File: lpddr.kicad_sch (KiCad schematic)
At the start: 37 parts, among them U1 MPFS250T-FCVG484, U12 MT53D512M32D2_WFBGA

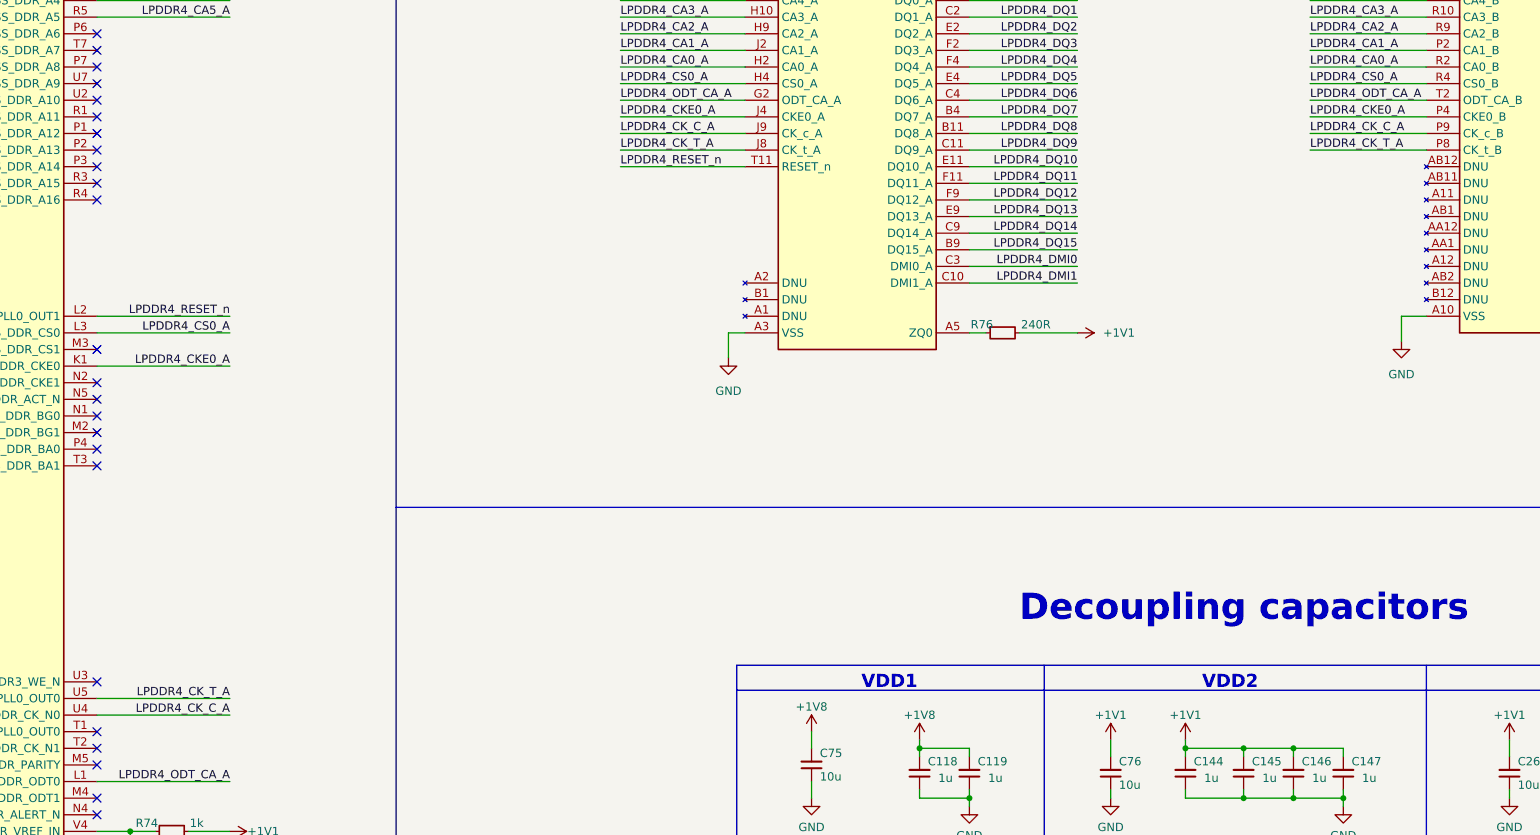
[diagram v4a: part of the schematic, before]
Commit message: [#56715] LPDDR4 match LS signals
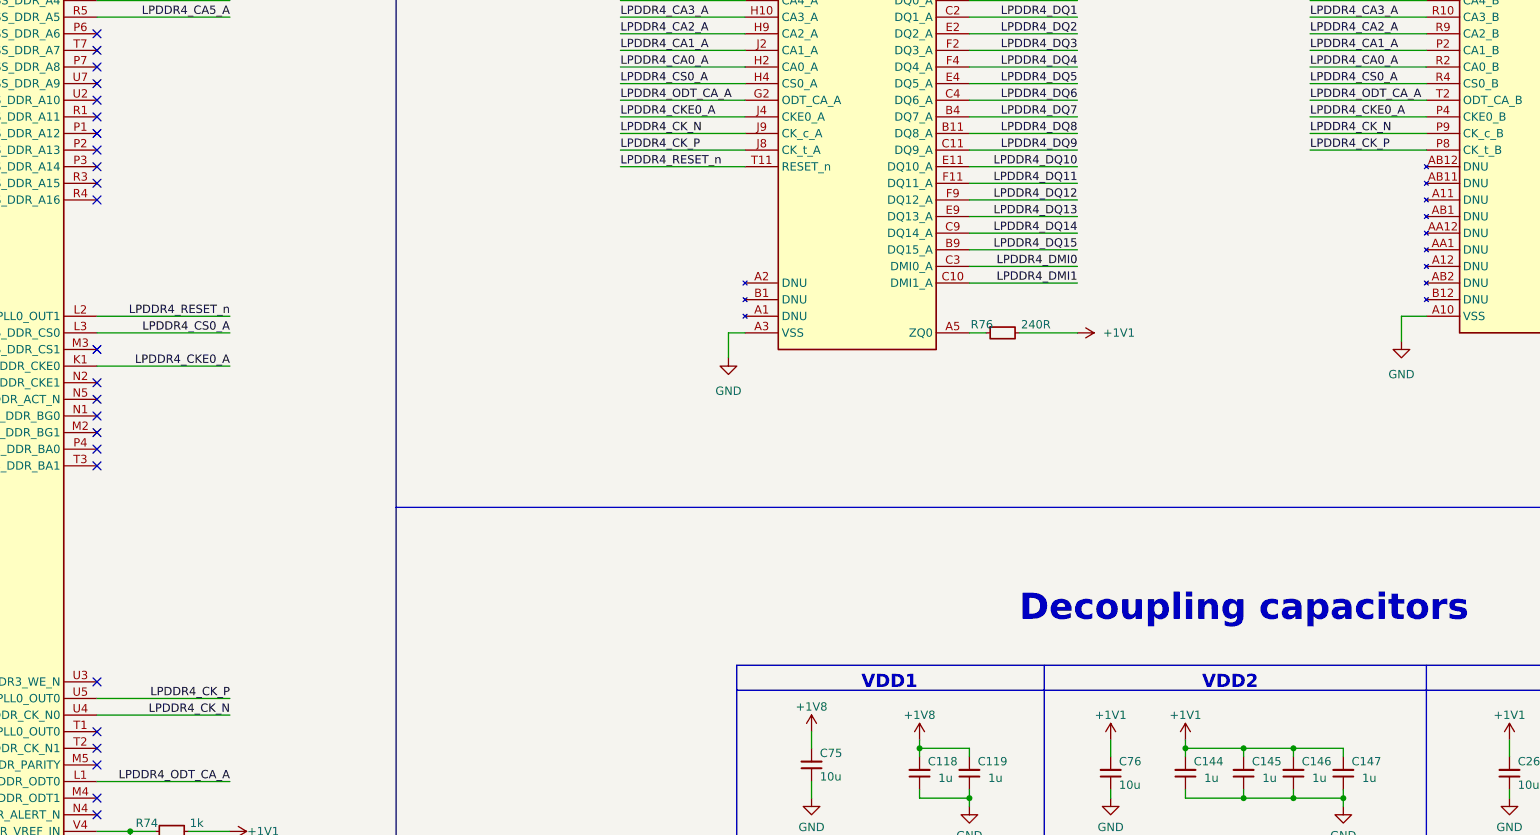
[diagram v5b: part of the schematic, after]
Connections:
- net LPDDR4_CK_C_A renamed LPDDR4_CK_N
- net LPDDR4_CK_T_A renamed LPDDR4_CK_P
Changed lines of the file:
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@@
-    (effects (font (size 1.27 1.27)) (justify left bottom))
-  )
-  (label "LPDDR4_CK_C_A" (at 312.42 96.52 0) (fields_autoplaced)
     (effects (font (size 1.27 1.27)) (justify left bottom))
   )
@@
     (effects (font (size 1.27 1.27)) (justify left bottom))
   )
+  (label "LPDDR4_CK_N" (at 207.01 96.52 0) (fields_autoplaced)
+    (effects (font (size 1.27 1.27)) (justify left bottom))
+  )
   (label "LPDDR4_DQ21" (at 45.72 139.7 0) (fields_autoplaced)
     (effects (font (size 1.27 1.27)) (justify left bottom))
@@
     (effects (font (size 1.27 1.27)) (justify left bottom))
   )
-  (label "LPDDR4_CK_C_A" (at 207.01 96.52 0) (fields_autoplaced)
-    (effects (font (size 1.27 1.27)) (justify left bottom))
-  )
-  (label "LPDDR4_CK_T_A" (at 312.42 99.06 0) (fields_autoplaced)
-    (effects (font (size 1.27 1.27)) (justify left bottom))
-  )
   (label "LPDDR4_DQS0_P" (at 276.86 68.58 180) (fields_autoplaced)
     (effects (font (size 1.27 1.27)) (justify right bottom))
@@
     (effects (font (size 1.27 1.27)) (justify right bottom))
   )
+  (label "LPDDR4_CK_N" (at 312.42 96.52 0) (fields_autoplaced)
+    (effects (font (size 1.27 1.27)) (justify left bottom))
+  )
   (label "LPDDR4_RESET_n" (at 207.01 101.6 0) (fields_autoplaced)
     (effects (font (size 1.27 1.27)) (justify left bottom))
@@
     (effects (font (size 1.27 1.27)) (justify left bottom))
   )
+  (label "LPDDR4_CK_P" (at 312.42 99.06 0) (fields_autoplaced)
+    (effects (font (size 1.27 1.27)) (justify left bottom))
+  )
   (label "LPDDR4_DQ12" (at 45.72 106.68 0) (fields_autoplaced)
     (effects (font (size 1.27 1.27)) (justify left bottom))
@@
     (effects (font (size 1.27 1.27)) (justify right bottom))
   )
+  (label "LPDDR4_CK_P" (at 207.01 99.06 0) (fields_autoplaced)
+    (effects (font (size 1.27 1.27)) (justify left bottom))
+  )
   (label "LPDDR4_DQ23" (at 381 93.98 180) (fields_autoplaced)
     (effects (font (size 1.27 1.27)) (justify right bottom))
@@
     (effects (font (size 1.27 1.27)) (justify left bottom))
   )
-  (label "LPDDR4_CK_T_A" (at 207.01 99.06 0) (fields_autoplaced)
-    (effects (font (size 1.27 1.27)) (justify left bottom))
-  )
   (label "LPDDR4_DQ25" (at 45.72 160.02 0) (fields_autoplaced)
     (effects (font (size 1.27 1.27)) (justify left bottom))
@@
     (effects (font (size 1.27 1.27)) (justify left bottom))
   )
-  (label "LPDDR4_CK_C_A" (at 147.32 185.42 180) (fields_autoplaced)
+  (label "LPDDR4_CK_N" (at 147.32 185.42 180) (fields_autoplaced)
     (effects (font (size 1.27 1.27)) (justify right bottom))
   )
@@
     (effects (font (size 1.27 1.27)) (justify right bottom))
   )
-  (label "LPDDR4_CK_T_A" (at 147.32 182.88 180) (fields_autoplaced)
-    (effects (font (size 1.27 1.27)) (justify right bottom))
-  )
+  (label "LPDDR4_CK_P" (at 147.32 182.88 180) (fields_autoplaced)
+    (effects (font (size 1.27 1.27)) (justify right bottom))
+  )

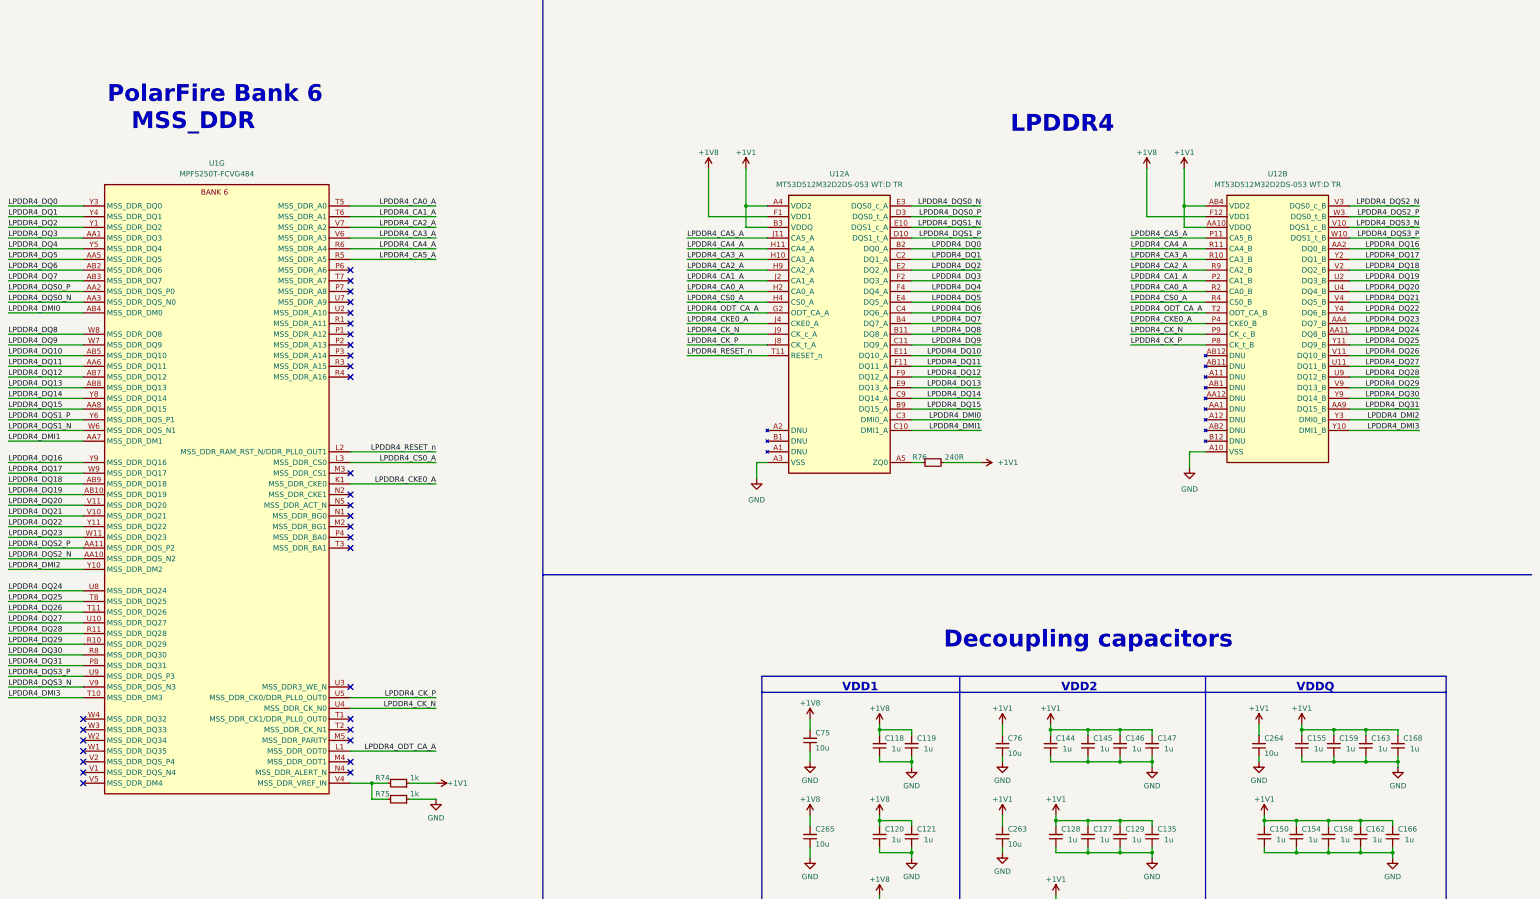
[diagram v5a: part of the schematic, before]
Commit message: [#57505] Start reworking schematic to hierarchical structure
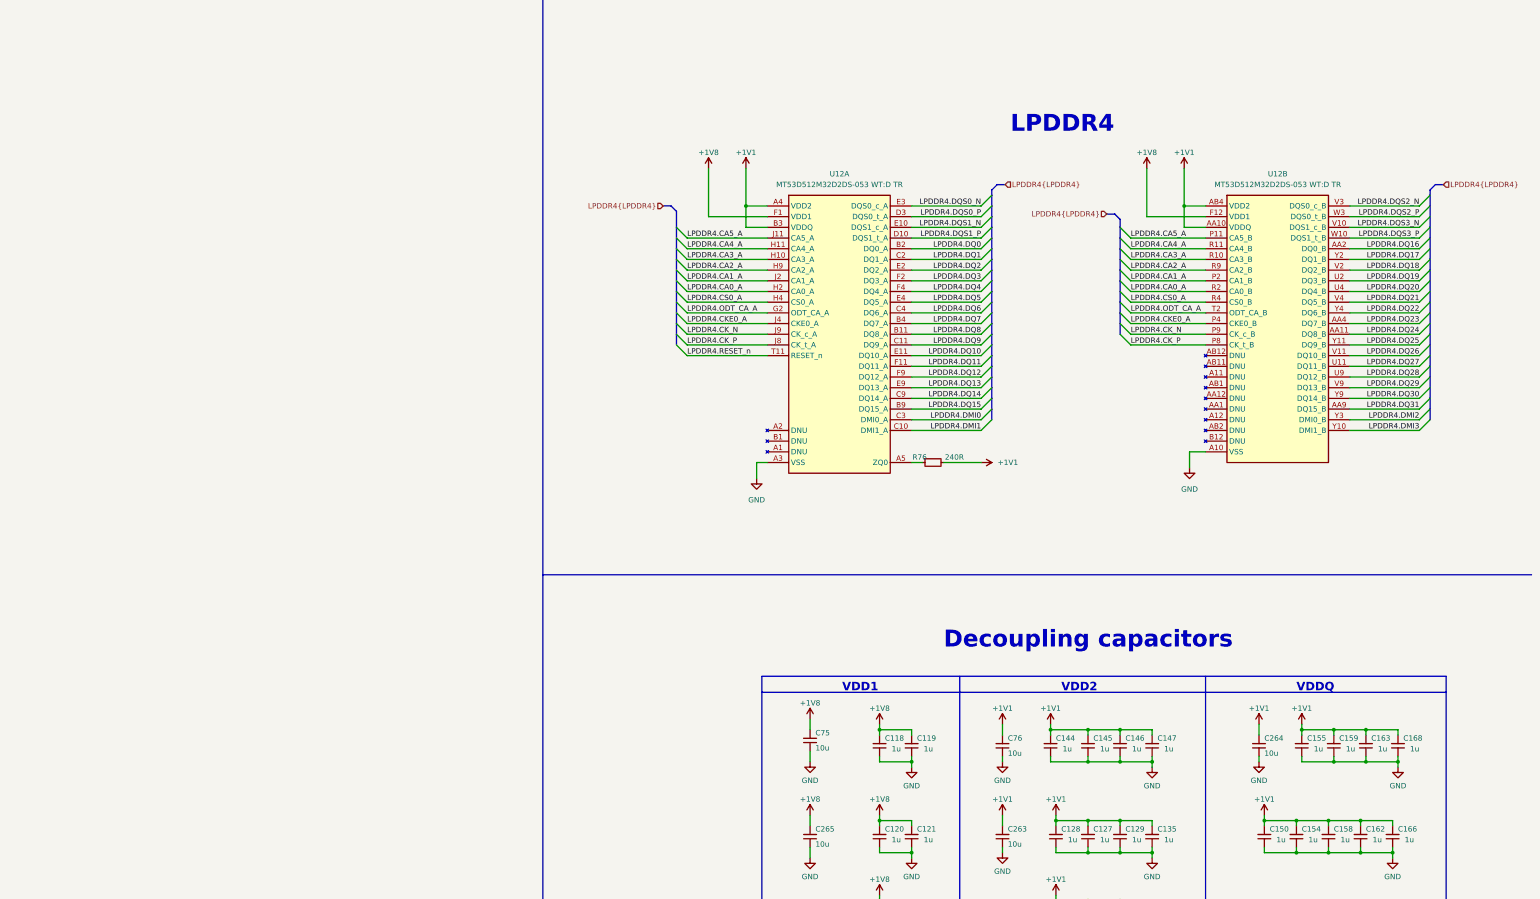
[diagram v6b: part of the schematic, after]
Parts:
- removed R74, R75: R_1k_0402, antmicro-footprints:R_0402_1005Metric, symbol antmicroResistors0402:R_1k_0402
- removed U1: MPFS250T-FCVG484, antmicro-footprints:BGA-484_19x19mm_Layout22x22_P0.8mm-microchip-technology-mpfs250t-fcvg484, symbol antmicroFPGAChips:MPFS250T-FCVG484
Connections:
- net LPDDR4_CA0_A renamed LPDDR4.CA0_A
- net LPDDR4_CA1_A renamed LPDDR4.CA1_A
- net LPDDR4_CA2_A renamed LPDDR4.CA2_A
- net LPDDR4_CA3_A renamed LPDDR4.CA3_A
- net LPDDR4_CA4_A renamed LPDDR4.CA4_A
- net LPDDR4_CA5_A renamed LPDDR4.CA5_A
- net LPDDR4_CKE0_A renamed LPDDR4.CKE0_A
- net LPDDR4_CK_N renamed LPDDR4.CK_N
- net LPDDR4_CK_P renamed LPDDR4.CK_P
- net LPDDR4_CS0_A renamed LPDDR4.CS0_A
- net LPDDR4_DMI0 renamed LPDDR4.DMI0
- net LPDDR4_DMI1 renamed LPDDR4.DMI1
- net LPDDR4_DMI2 renamed LPDDR4.DMI2
- net LPDDR4_DMI3 renamed LPDDR4.DMI3
- net LPDDR4_DQ0 renamed LPDDR4.DQ0
- net LPDDR4_DQ1 renamed LPDDR4.DQ1
- net LPDDR4_DQ10 renamed LPDDR4.DQ10
- net LPDDR4_DQ11 renamed LPDDR4.DQ11
- net LPDDR4_DQ12 renamed LPDDR4.DQ12
- net LPDDR4_DQ13 renamed LPDDR4.DQ13
- net LPDDR4_DQ14 renamed LPDDR4.DQ14
- net LPDDR4_DQ15 renamed LPDDR4.DQ15
- net LPDDR4_DQ16 renamed LPDDR4.DQ16
- net LPDDR4_DQ17 renamed LPDDR4.DQ17
- net LPDDR4_DQ18 renamed LPDDR4.DQ18
- net LPDDR4_DQ19 renamed LPDDR4.DQ19
- net LPDDR4_DQ2 renamed LPDDR4.DQ2
- net LPDDR4_DQ20 renamed LPDDR4.DQ20
- net LPDDR4_DQ21 renamed LPDDR4.DQ21
- net LPDDR4_DQ22 renamed LPDDR4.DQ22
- net LPDDR4_DQ23 renamed LPDDR4.DQ23
- net LPDDR4_DQ24 renamed LPDDR4.DQ24
- net LPDDR4_DQ25 renamed LPDDR4.DQ25
- net LPDDR4_DQ26 renamed LPDDR4.DQ26
- net LPDDR4_DQ27 renamed LPDDR4.DQ27
- net LPDDR4_DQ28 renamed LPDDR4.DQ28
- net LPDDR4_DQ29 renamed LPDDR4.DQ29
- net LPDDR4_DQ3 renamed LPDDR4.DQ3
- net LPDDR4_DQ30 renamed LPDDR4.DQ30
- net LPDDR4_DQ31 renamed LPDDR4.DQ31
- net LPDDR4_DQ4 renamed LPDDR4.DQ4
- net LPDDR4_DQ5 renamed LPDDR4.DQ5
- net LPDDR4_DQ6 renamed LPDDR4.DQ6
- net LPDDR4_DQ7 renamed LPDDR4.DQ7
- net LPDDR4_DQ8 renamed LPDDR4.DQ8
- net LPDDR4_DQ9 renamed LPDDR4.DQ9
- net LPDDR4_DQS0_N renamed LPDDR4.DQS0_N
- net LPDDR4_DQS0_P renamed LPDDR4.DQS0_P
- net LPDDR4_DQS1_N renamed LPDDR4.DQS1_N
- net LPDDR4_DQS1_P renamed LPDDR4.DQS1_P
- net LPDDR4_DQS2_N renamed LPDDR4.DQS2_N
- net LPDDR4_DQS2_P renamed LPDDR4.DQS2_P
- net LPDDR4_DQS3_N renamed LPDDR4.DQS3_N
- net LPDDR4_DQS3_P renamed LPDDR4.DQS3_P
- net LPDDR4_ODT_CA_A renamed LPDDR4.ODT_CA_A
- net LPDDR4_RESET_n renamed LPDDR4.RESET_n
- no-connect marks 31 -> 0
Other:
- note removed: "PolarFire Bank 6 MSS_DDR"
